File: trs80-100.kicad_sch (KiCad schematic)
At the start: 110 parts, among them J1 Adapter Jack CN9, M27 4011, M28 4013, SW3 SLB-22BP-03, SW4 Reset Switch, SW5 SSP32201, T10 2SC2603, T11 2SC2603, T13 2SC2603(E), T14 2SC2603(E), T15 2SC2603(E), T16 2SC2603(E), T17 2SC2603(E), T18 2SC2603, T19 2SA1115, T20 2SC2603, T21 2SC2603(E), T22 2SC2603(E), T25 2SC2603, T27 2SC2603, T28 2SA1115, T9 2SC2603

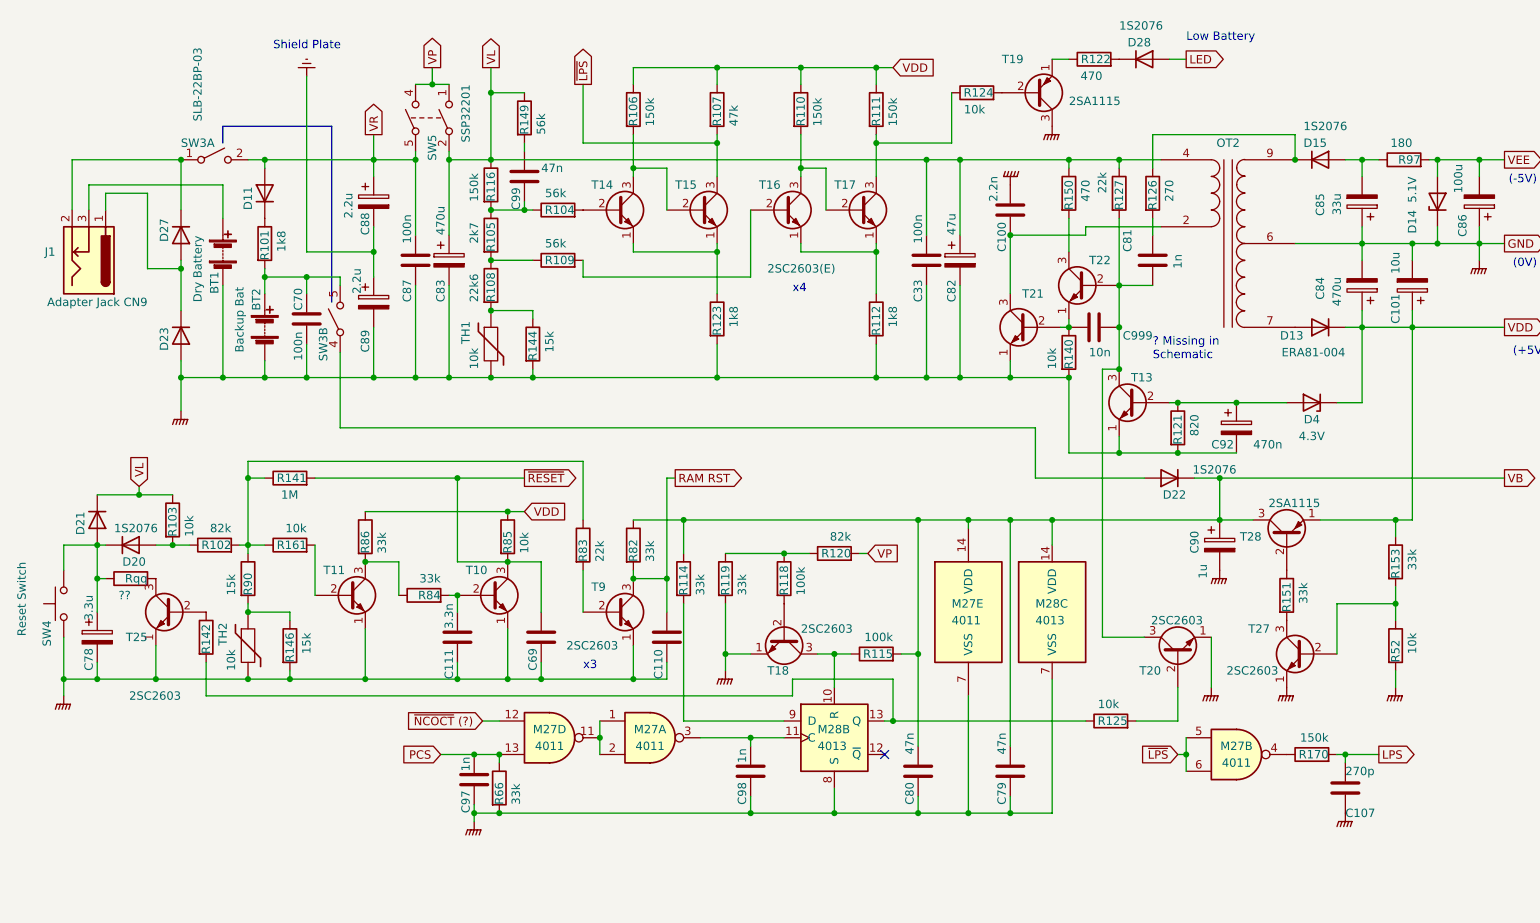
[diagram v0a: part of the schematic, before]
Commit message: Move value inside resistor rectangle.
Also
 * Fix a few transcribe errors.
 * Augment values found in the component list.
 * Remove pin numbers from transistors.
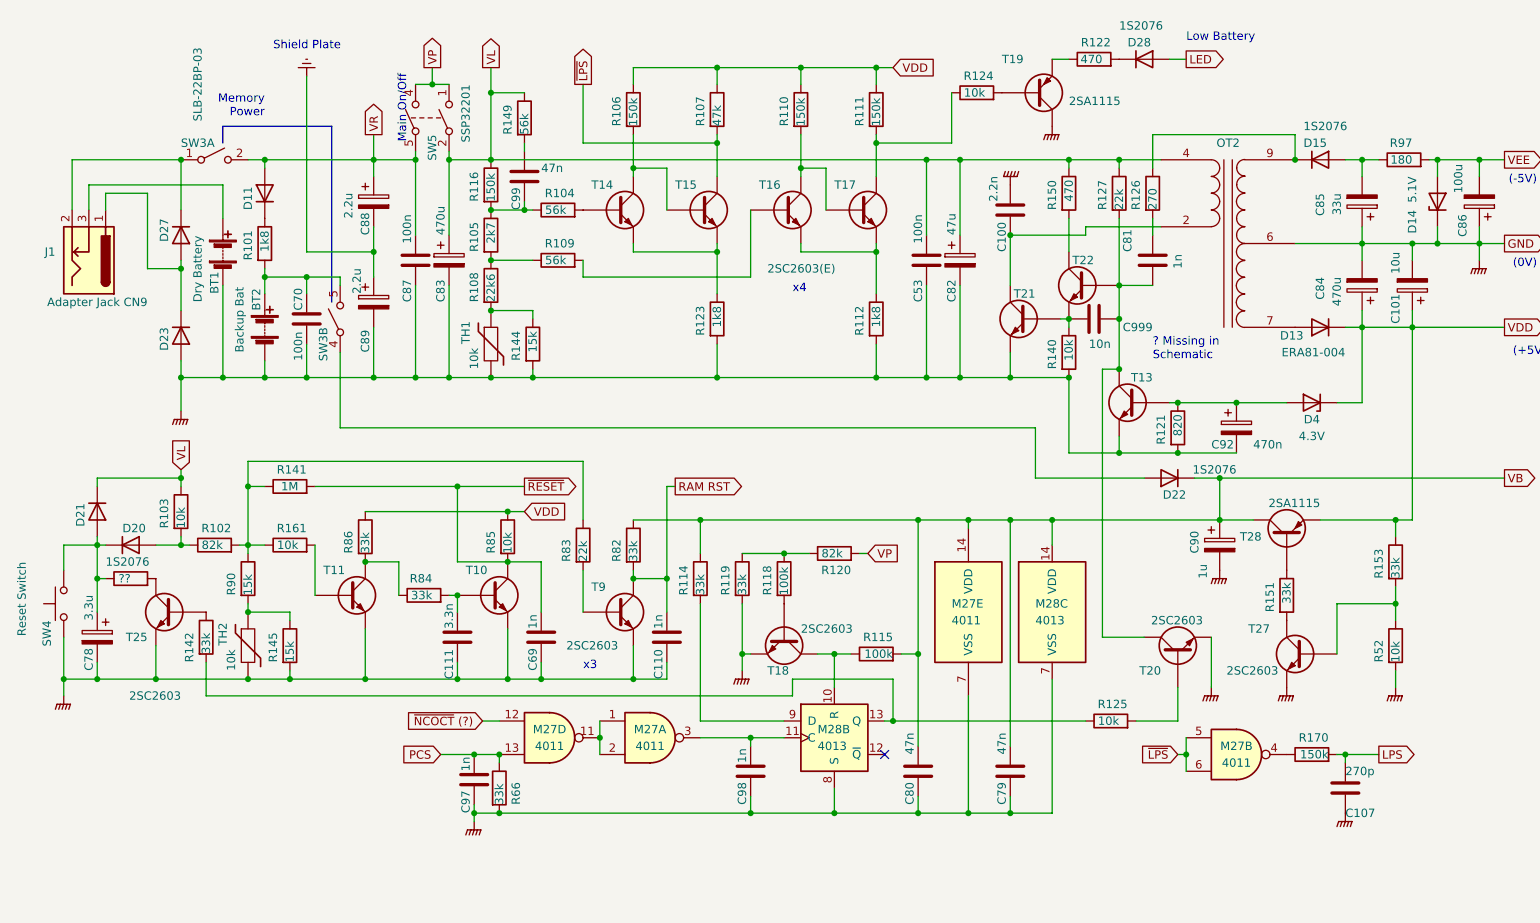
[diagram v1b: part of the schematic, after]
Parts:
- C110, C69: value 3.3n -> 1n
- R142: value 10k -> 33k
- renumbered C33 to C53, R146 to R145
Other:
- note added: "Main On/Off"
- note added: "Memory Power"
- company: (none) -> Transcribed by Henner Zeller
- moved on the sheet: C999, D21, R103, R114, R119, R141

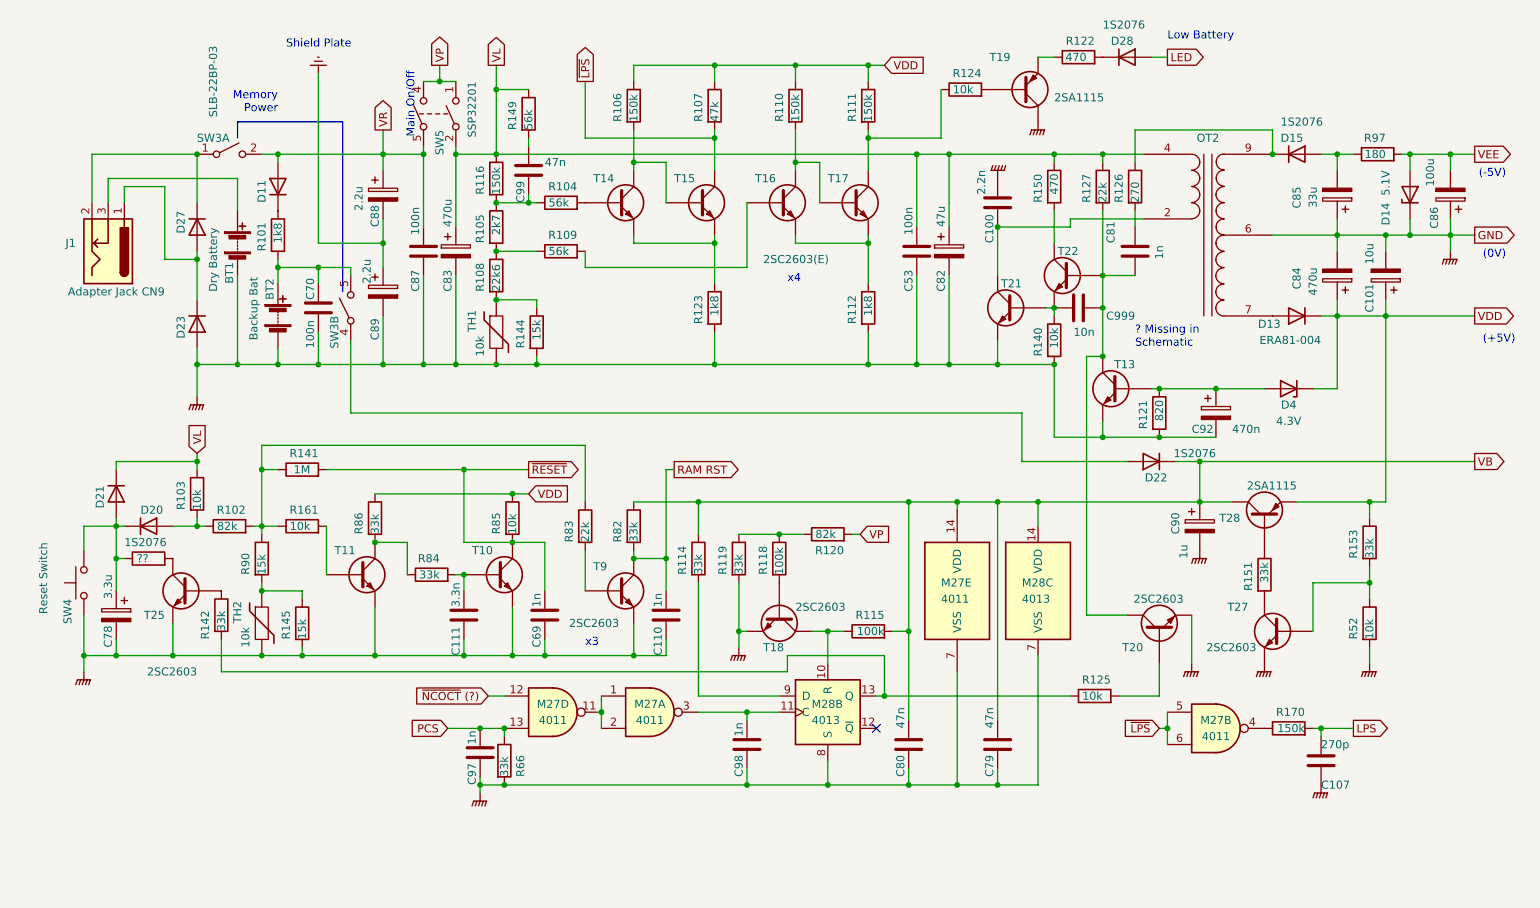
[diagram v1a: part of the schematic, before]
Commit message: Center values and designator in resistors. Center designator in Diodes.
Also add missing ferrite beads and fuses to the input jack.
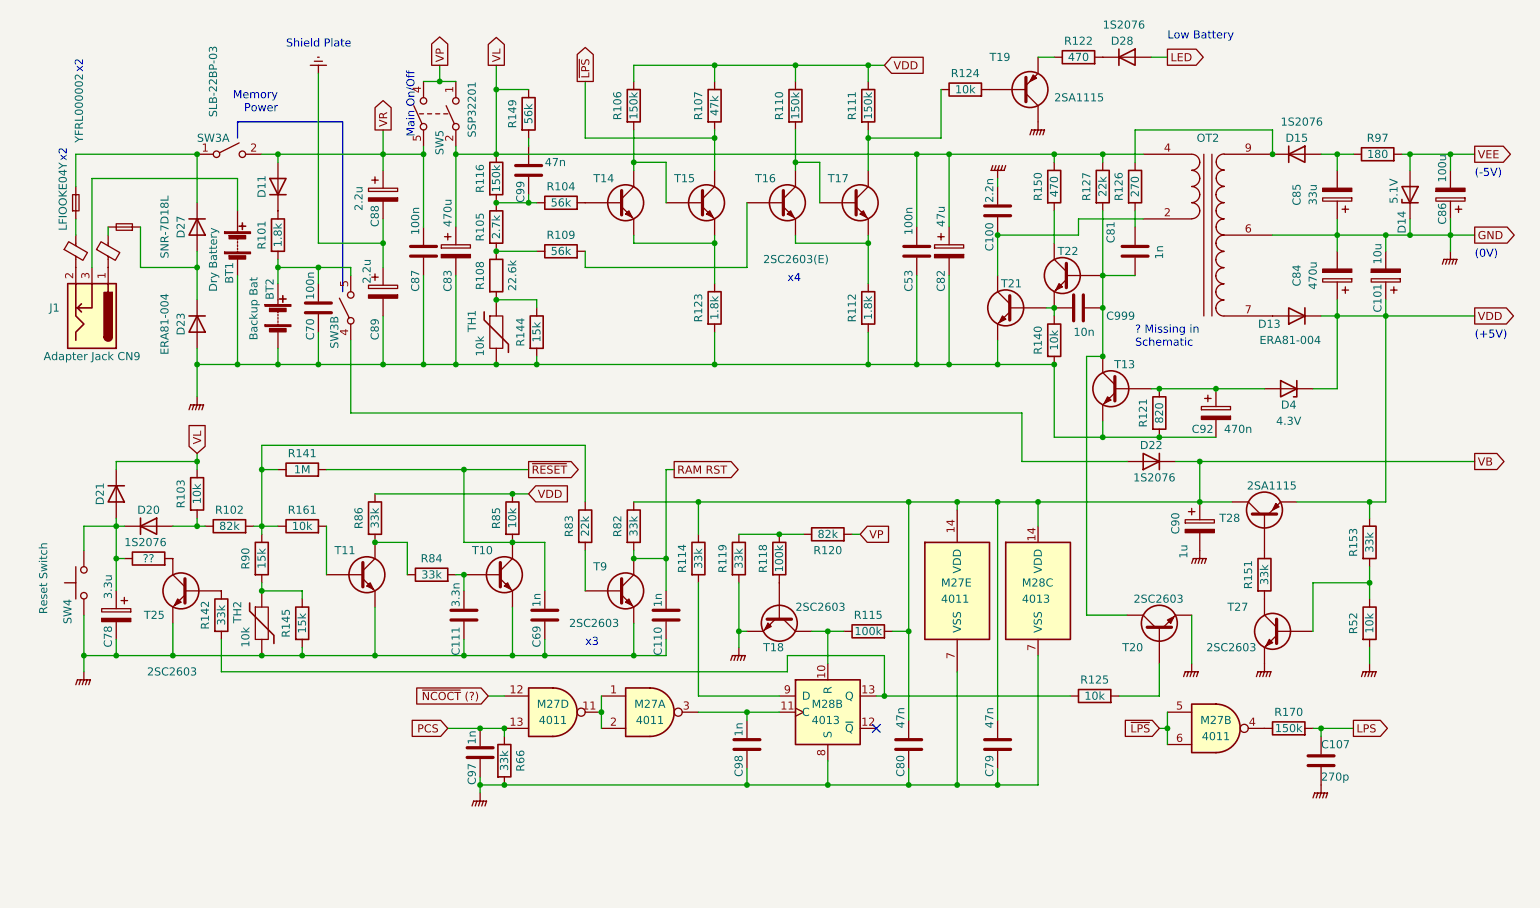
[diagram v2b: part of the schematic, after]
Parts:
- added F1, F2: LFIOOKE04Y, symbol Device:Fuse_Small
- added FB1, FB2: YFRL000002, symbol Device:FerriteBead_Small
- R101, R112, R123: value 1k8 -> 1.8k
- R105: value 2k7 -> 2.7k
- R108: value 22k6 -> 22.6k
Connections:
- net at D27.1 (K), SW3.1 (A): now also F1.2; no longer J1.2
- net at D23.1 (K), D27.2 (A): now also F2.1; no longer J1.1
- new net: F1.1, FB1.1
- new net: F2.2, FB2.1
- new net: FB1.2, J1.2
- new net: FB2.2, J1.1
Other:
- note added: "x2"
- moved on the sheet: C100, J1
